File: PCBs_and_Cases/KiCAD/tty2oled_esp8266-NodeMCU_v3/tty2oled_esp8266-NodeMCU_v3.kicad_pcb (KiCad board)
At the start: 2 copper layers, 35.6 x 99.7 mm, 2 parts

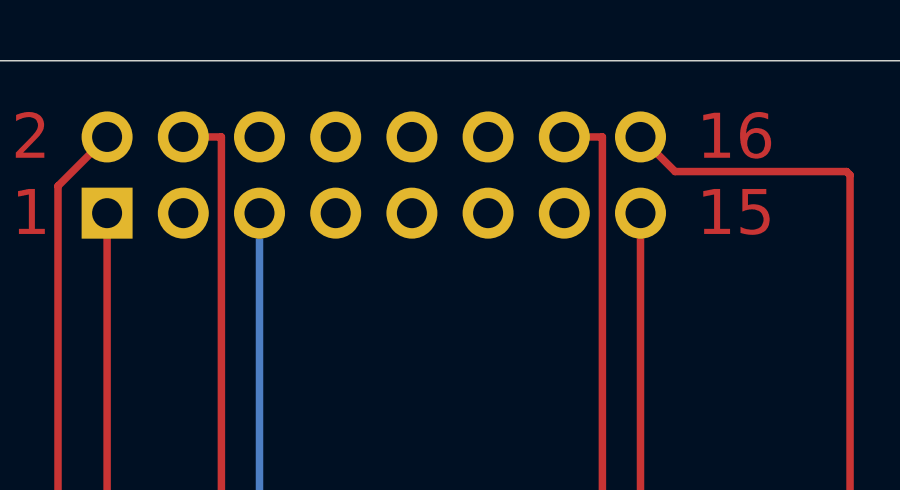
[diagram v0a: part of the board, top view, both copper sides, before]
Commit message: KiCAD: GNDs added, files renamed
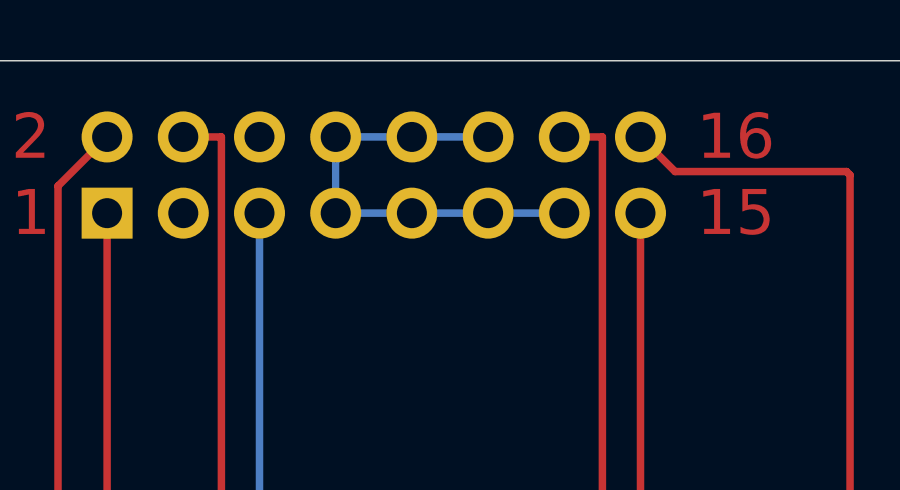
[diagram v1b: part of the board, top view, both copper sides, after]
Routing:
- net (no net): track 536.3 -> 551.6 mm
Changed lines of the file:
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@@
     (thickness 1.6)
     (drawings 9)
-    (tracks 31)
+    (tracks 34)
     (zones 0)
     (modules 2)
@@
       (effects (font (size 1 1) (thickness 0.15)))
     )
+    (fp_line (start 15.25 26.5) (end 15.25 -30.5) (layer F.SilkS) (width 0.15))
+    (fp_line (start -15.25 26.5) (end 15.25 26.5) (layer F.SilkS) (width 0.15))
+    (fp_line (start -15.25 -30.5) (end -15.25 26.5) (layer F.SilkS) (width 0.15))
+    (fp_line (start -14.75 -30.5) (end -15.25 -30.5) (layer F.SilkS) (width 0.15))
+    (fp_line (start 15.25 -30.5) (end -14.75 -30.5) (layer F.SilkS) (width 0.15))
+    (fp_circle (center 12.7 -27.94) (end 13.97 -29.21) (layer F.SilkS) (width 0.15))
+    (fp_circle (center -12.7 -27.94) (end -11.43 -29.21) (layer F.SilkS) (width 0.15))
+    (fp_circle (center -12.7 24.13) (end -11.43 22.86) (layer F.SilkS) (width 0.15))
+    (fp_circle (center 12.7 24.13) (end 13.97 22.86) (layer F.SilkS) (width 0.15))
     (fp_text user D0 (at 11.43 -20.32) (layer F.SilkS)
       (effects (font (size 1 1) (thickness 0.15)))
@@
       (effects (font (size 1 1) (thickness 0.15)))
     )
-    (fp_circle (center 12.7 24.13) (end 13.97 22.86) (layer F.SilkS) (width 0.15))
-    (fp_circle (center -12.7 24.13) (end -11.43 22.86) (layer F.SilkS) (width 0.15))
-    (fp_circle (center -12.7 -27.94) (end -11.43 -29.21) (layer F.SilkS) (width 0.15))
-    (fp_circle (center 12.7 -27.94) (end 13.97 -29.21) (layer F.SilkS) (width 0.15))
-    (fp_line (start 15.25 -30.5) (end -14.75 -30.5) (layer F.SilkS) (width 0.15))
-    (fp_line (start -14.75 -30.5) (end -15.25 -30.5) (layer F.SilkS) (width 0.15))
-    (fp_line (start -15.25 -30.5) (end -15.25 26.5) (layer F.SilkS) (width 0.15))
-    (fp_line (start -15.25 26.5) (end 15.25 26.5) (layer F.SilkS) (width 0.15))
-    (fp_line (start 15.25 26.5) (end 15.25 -30.5) (layer F.SilkS) (width 0.15))
     (pad 30 thru_hole circle (at 13.97 -20.32) (size 1.524 1.524) (drill 0.762) (layers *.Cu *.Mask F.SilkS))
     (pad 29 thru_hole circle (at 13.97 -17.78) (size 1.524 1.524) (drill 0.762) (layers *.Cu *.Mask F.SilkS))
@@
       (effects (font (size 1 1) (thickness 0.15)) (justify mirror))
     )
+    (fp_line (start 0 1.27) (end 3.81 1.27) (layer B.Fab) (width 0.1))
+    (fp_line (start 3.81 1.27) (end 3.81 -19.05) (layer B.Fab) (width 0.1))
+    (fp_line (start 3.81 -19.05) (end -1.27 -19.05) (layer B.Fab) (width 0.1))
+    (fp_line (start -1.27 -19.05) (end -1.27 0) (layer B.Fab) (width 0.1))
+    (fp_line (start -1.27 0) (end 0 1.27) (layer B.Fab) (width 0.1))
+    (fp_line (start -1.33 -19.11) (end 3.87 -19.11) (layer B.SilkS) (width 0.12))
+    (fp_line (start -1.33 -1.27) (end -1.33 -19.11) (layer B.SilkS) (width 0.12))
+    (fp_line (start 3.87 1.33) (end 3.87 -19.11) (layer B.SilkS) (width 0.12))
+    (fp_line (start -1.33 -1.27) (end 1.27 -1.27) (layer B.SilkS) (width 0.12))
+    (fp_line (start 1.27 -1.27) (end 1.27 1.33) (layer B.SilkS) (width 0.12))
+    (fp_line (start 1.27 1.33) (end 3.87 1.33) (layer B.SilkS) (width 0.12))
+    (fp_line (start -1.33 0) (end -1.33 1.33) (layer B.SilkS) (width 0.12))
+    (fp_line (start -1.33 1.33) (end 0 1.33) (layer B.SilkS) (width 0.12))
+    (fp_line (start -1.8 1.8) (end -1.8 -19.55) (layer B.CrtYd) (width 0.05))
+    (fp_line (start -1.8 -19.55) (end 4.35 -19.55) (layer B.CrtYd) (width 0.05))
+    (fp_line (start 4.35 -19.55) (end 4.35 1.8) (layer B.CrtYd) (width 0.05))
     (fp_line (start 4.35 1.8) (end -1.8 1.8) (layer B.CrtYd) (width 0.05))
-    (fp_line (start 4.35 -19.55) (end 4.35 1.8) (layer B.CrtYd) (width 0.05))
-    (fp_line (start -1.8 -19.55) (end 4.35 -19.55) (layer B.CrtYd) (width 0.05))
-    (fp_line (start -1.8 1.8) (end -1.8 -19.55) (layer B.CrtYd) (width 0.05))
-    (fp_line (start -1.33 1.33) (end 0 1.33) (layer B.SilkS) (width 0.12))
-    (fp_line (start -1.33 0) (end -1.33 1.33) (layer B.SilkS) (width 0.12))
-    (fp_line (start 1.27 1.33) (end 3.87 1.33) (layer B.SilkS) (width 0.12))
-    (fp_line (start 1.27 -1.27) (end 1.27 1.33) (layer B.SilkS) (width 0.12))
-    (fp_line (start -1.33 -1.27) (end 1.27 -1.27) (layer B.SilkS) (width 0.12))
-    (fp_line (start 3.87 1.33) (end 3.87 -19.11) (layer B.SilkS) (width 0.12))
-    (fp_line (start -1.33 -1.27) (end -1.33 -19.11) (layer B.SilkS) (width 0.12))
-    (fp_line (start -1.33 -19.11) (end 3.87 -19.11) (layer B.SilkS) (width 0.12))
-    (fp_line (start -1.27 0) (end 0 1.27) (layer B.Fab) (width 0.1))
-    (fp_line (start -1.27 -19.05) (end -1.27 0) (layer B.Fab) (width 0.1))
-    (fp_line (start 3.81 -19.05) (end -1.27 -19.05) (layer B.Fab) (width 0.1))
-    (fp_line (start 3.81 1.27) (end 3.81 -19.05) (layer B.Fab) (width 0.1))
-    (fp_line (start 0 1.27) (end 3.81 1.27) (layer B.Fab) (width 0.1))
     (fp_text user %R (at 1.27 -8.89 180) (layer B.Fab)
       (effects (font (size 1 1) (thickness 0.15)) (justify mirror))
@@
   (segment (start 157.48 53.975) (end 157.48 103.505) (width 0.25) (layer F.Cu) (net 0))
   (segment (start 165.735 55.245) (end 165.735 127.635) (width 0.25) (layer F.Cu) (net 0))
+  (segment (start 156.21 56.515) (end 148.59 56.515) (width 0.25) (layer B.Cu) (net 0))
+  (segment (start 148.59 56.515) (end 148.59 53.975) (width 0.25) (layer B.Cu) (net 0))
+  (segment (start 148.59 53.975) (end 153.67 53.975) (width 0.25) (layer B.Cu) (net 0))
 )

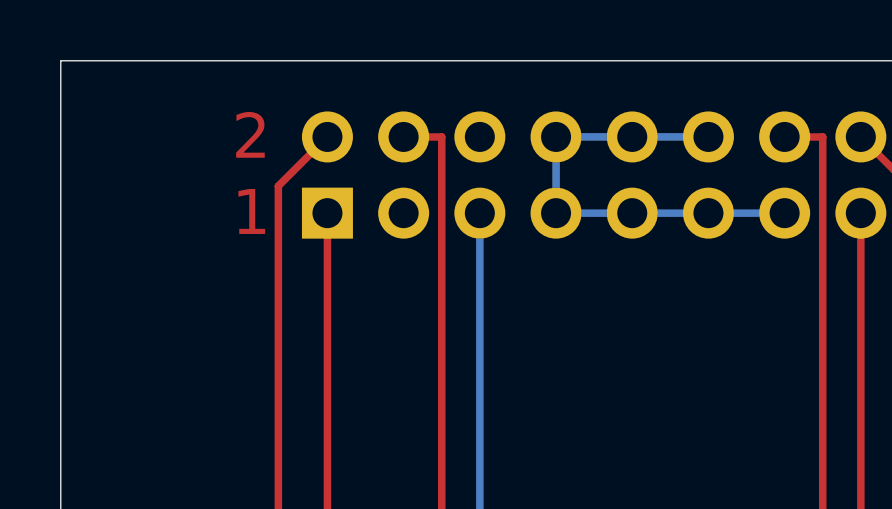
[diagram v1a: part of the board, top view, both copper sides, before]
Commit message: GND was missing in KiCAD/Gerbers
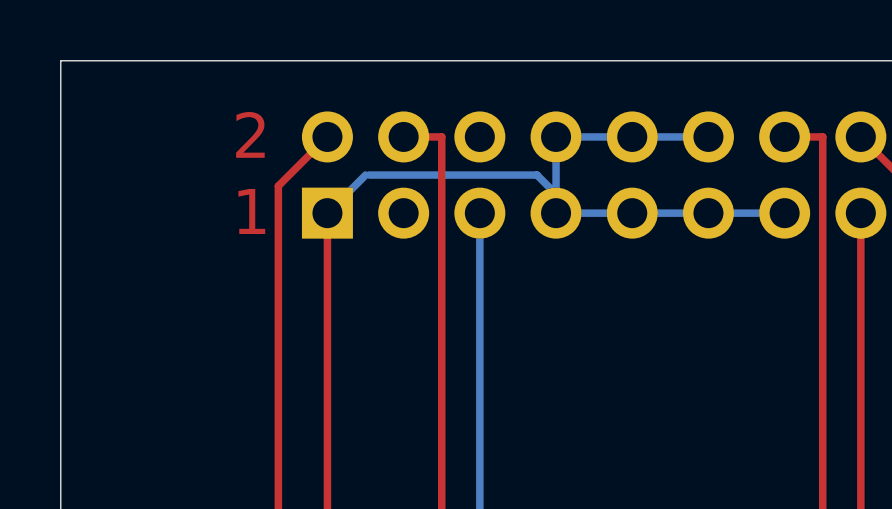
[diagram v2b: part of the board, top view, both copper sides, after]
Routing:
- net (no net): track 551.6 -> 560.5 mm
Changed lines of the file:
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@@
     (thickness 1.6)
     (drawings 9)
-    (tracks 34)
+    (tracks 38)
     (zones 0)
     (modules 2)
@@
       (effects (font (size 1 1) (thickness 0.15)))
     )
+    (fp_circle (center 12.7 24.13) (end 13.97 22.86) (layer F.SilkS) (width 0.15))
+    (fp_circle (center -12.7 24.13) (end -11.43 22.86) (layer F.SilkS) (width 0.15))
+    (fp_circle (center -12.7 -27.94) (end -11.43 -29.21) (layer F.SilkS) (width 0.15))
+    (fp_circle (center 12.7 -27.94) (end 13.97 -29.21) (layer F.SilkS) (width 0.15))
+    (fp_line (start 15.25 -30.5) (end -14.75 -30.5) (layer F.SilkS) (width 0.15))
+    (fp_line (start -14.75 -30.5) (end -15.25 -30.5) (layer F.SilkS) (width 0.15))
+    (fp_line (start -15.25 -30.5) (end -15.25 26.5) (layer F.SilkS) (width 0.15))
+    (fp_line (start -15.25 26.5) (end 15.25 26.5) (layer F.SilkS) (width 0.15))
     (fp_line (start 15.25 26.5) (end 15.25 -30.5) (layer F.SilkS) (width 0.15))
-    (fp_line (start -15.25 26.5) (end 15.25 26.5) (layer F.SilkS) (width 0.15))
-    (fp_line (start -15.25 -30.5) (end -15.25 26.5) (layer F.SilkS) (width 0.15))
-    (fp_line (start -14.75 -30.5) (end -15.25 -30.5) (layer F.SilkS) (width 0.15))
-    (fp_line (start 15.25 -30.5) (end -14.75 -30.5) (layer F.SilkS) (width 0.15))
-    (fp_circle (center 12.7 -27.94) (end 13.97 -29.21) (layer F.SilkS) (width 0.15))
-    (fp_circle (center -12.7 -27.94) (end -11.43 -29.21) (layer F.SilkS) (width 0.15))
-    (fp_circle (center -12.7 24.13) (end -11.43 22.86) (layer F.SilkS) (width 0.15))
-    (fp_circle (center 12.7 24.13) (end 13.97 22.86) (layer F.SilkS) (width 0.15))
     (fp_text user D0 (at 11.43 -20.32) (layer F.SilkS)
       (effects (font (size 1 1) (thickness 0.15)))
@@
       (effects (font (size 1 1) (thickness 0.15)) (justify mirror))
     )
+    (fp_line (start 4.35 1.8) (end -1.8 1.8) (layer B.CrtYd) (width 0.05))
+    (fp_line (start 4.35 -19.55) (end 4.35 1.8) (layer B.CrtYd) (width 0.05))
+    (fp_line (start -1.8 -19.55) (end 4.35 -19.55) (layer B.CrtYd) (width 0.05))
+    (fp_line (start -1.8 1.8) (end -1.8 -19.55) (layer B.CrtYd) (width 0.05))
+    (fp_line (start -1.33 1.33) (end 0 1.33) (layer B.SilkS) (width 0.12))
+    (fp_line (start -1.33 0) (end -1.33 1.33) (layer B.SilkS) (width 0.12))
+    (fp_line (start 1.27 1.33) (end 3.87 1.33) (layer B.SilkS) (width 0.12))
+    (fp_line (start 1.27 -1.27) (end 1.27 1.33) (layer B.SilkS) (width 0.12))
+    (fp_line (start -1.33 -1.27) (end 1.27 -1.27) (layer B.SilkS) (width 0.12))
+    (fp_line (start 3.87 1.33) (end 3.87 -19.11) (layer B.SilkS) (width 0.12))
+    (fp_line (start -1.33 -1.27) (end -1.33 -19.11) (layer B.SilkS) (width 0.12))
+    (fp_line (start -1.33 -19.11) (end 3.87 -19.11) (layer B.SilkS) (width 0.12))
+    (fp_line (start -1.27 0) (end 0 1.27) (layer B.Fab) (width 0.1))
+    (fp_line (start -1.27 -19.05) (end -1.27 0) (layer B.Fab) (width 0.1))
+    (fp_line (start 3.81 -19.05) (end -1.27 -19.05) (layer B.Fab) (width 0.1))
+    (fp_line (start 3.81 1.27) (end 3.81 -19.05) (layer B.Fab) (width 0.1))
     (fp_line (start 0 1.27) (end 3.81 1.27) (layer B.Fab) (width 0.1))
-    (fp_line (start 3.81 1.27) (end 3.81 -19.05) (layer B.Fab) (width 0.1))
-    (fp_line (start 3.81 -19.05) (end -1.27 -19.05) (layer B.Fab) (width 0.1))
-    (fp_line (start -1.27 -19.05) (end -1.27 0) (layer B.Fab) (width 0.1))
-    (fp_line (start -1.27 0) (end 0 1.27) (layer B.Fab) (width 0.1))
-    (fp_line (start -1.33 -19.11) (end 3.87 -19.11) (layer B.SilkS) (width 0.12))
-    (fp_line (start -1.33 -1.27) (end -1.33 -19.11) (layer B.SilkS) (width 0.12))
-    (fp_line (start 3.87 1.33) (end 3.87 -19.11) (layer B.SilkS) (width 0.12))
-    (fp_line (start -1.33 -1.27) (end 1.27 -1.27) (layer B.SilkS) (width 0.12))
-    (fp_line (start 1.27 -1.27) (end 1.27 1.33) (layer B.SilkS) (width 0.12))
-    (fp_line (start 1.27 1.33) (end 3.87 1.33) (layer B.SilkS) (width 0.12))
-    (fp_line (start -1.33 0) (end -1.33 1.33) (layer B.SilkS) (width 0.12))
-    (fp_line (start -1.33 1.33) (end 0 1.33) (layer B.SilkS) (width 0.12))
-    (fp_line (start -1.8 1.8) (end -1.8 -19.55) (layer B.CrtYd) (width 0.05))
-    (fp_line (start -1.8 -19.55) (end 4.35 -19.55) (layer B.CrtYd) (width 0.05))
-    (fp_line (start 4.35 -19.55) (end 4.35 1.8) (layer B.CrtYd) (width 0.05))
-    (fp_line (start 4.35 1.8) (end -1.8 1.8) (layer B.CrtYd) (width 0.05))
     (fp_text user %R (at 1.27 -8.89 180) (layer B.Fab)
       (effects (font (size 1 1) (thickness 0.15)) (justify mirror))
@@
   (segment (start 148.59 56.515) (end 148.59 53.975) (width 0.25) (layer B.Cu) (net 0))
   (segment (start 148.59 53.975) (end 153.67 53.975) (width 0.25) (layer B.Cu) (net 0))
+  (segment (start 140.97 56.515) (end 142.24 55.245) (width 0.25) (layer B.Cu) (net 0))
+  (segment (start 142.367 55.245) (end 147.955 55.245) (width 0.25) (layer B.Cu) (net 0))
+  (segment (start 148.59 55.88) (end 148.59 56.515) (width 0.25) (layer B.Cu) (net 0))
+  (segment (start 147.955 55.245) (end 148.59 55.88) (width 0.25) (layer B.Cu) (net 0))
 )

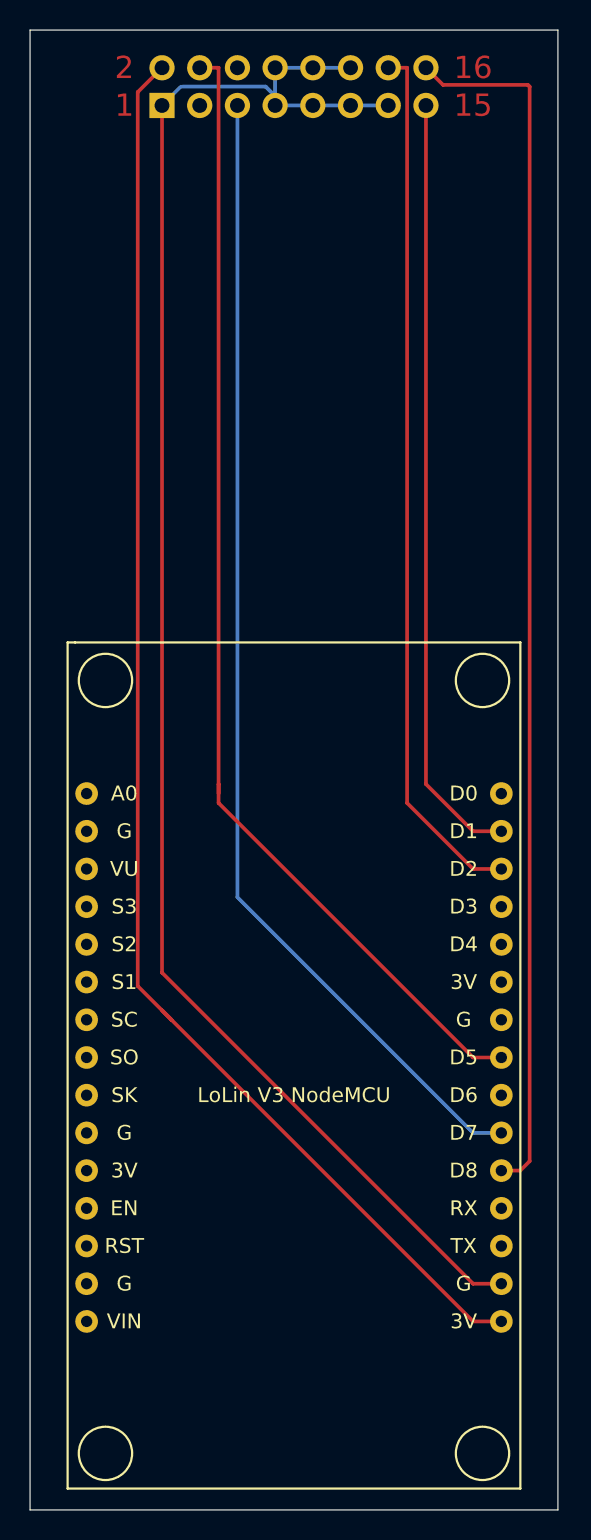
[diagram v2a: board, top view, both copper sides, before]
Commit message: ESP32-DevKitC removed, Lolin32 added
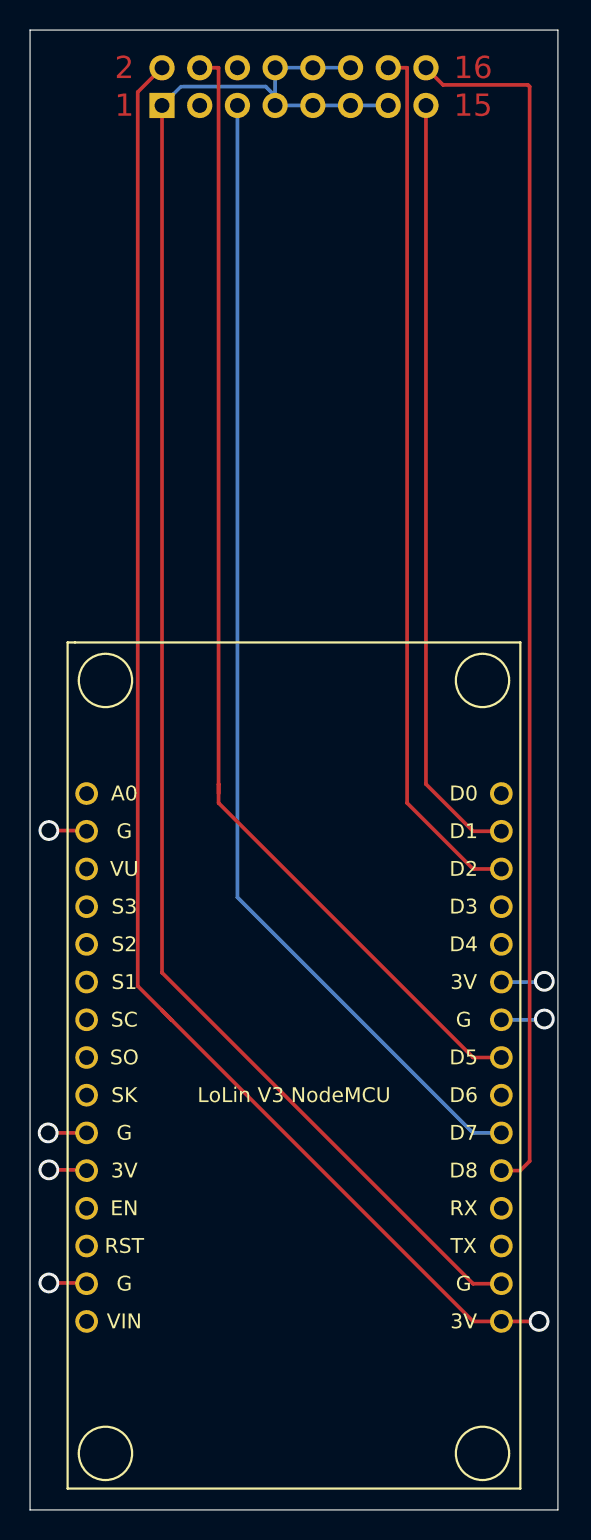
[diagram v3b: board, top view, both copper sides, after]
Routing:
- net (no net): track 560.5 -> 579.2 mm, vias 0 -> 7
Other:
- board text added: "3V"
- board text added: "G"
- board text added: "MiSTer_tty2oled Idea: LarsVenice Desgin: RealLarry"
- board text added: "Thanks to Sorgelig, Jukk@M, Jotego, tf_hh and all other developers"
- board text added: "v1.0"
